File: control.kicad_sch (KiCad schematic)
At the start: 16 parts, among them J1 Wurth_THR_Terminal_M4, J2 Wurth_THR_Terminal_M4, J3 Wurth_THR_Terminal_M4, J5 Conn_02x20_Odd_Even, J6 TE_Faston_20-16AWG_Straight_T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, J7 TE_Faston_20-16AWG_Straight_T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, U1 TPS7B8733, U2 MAX33071

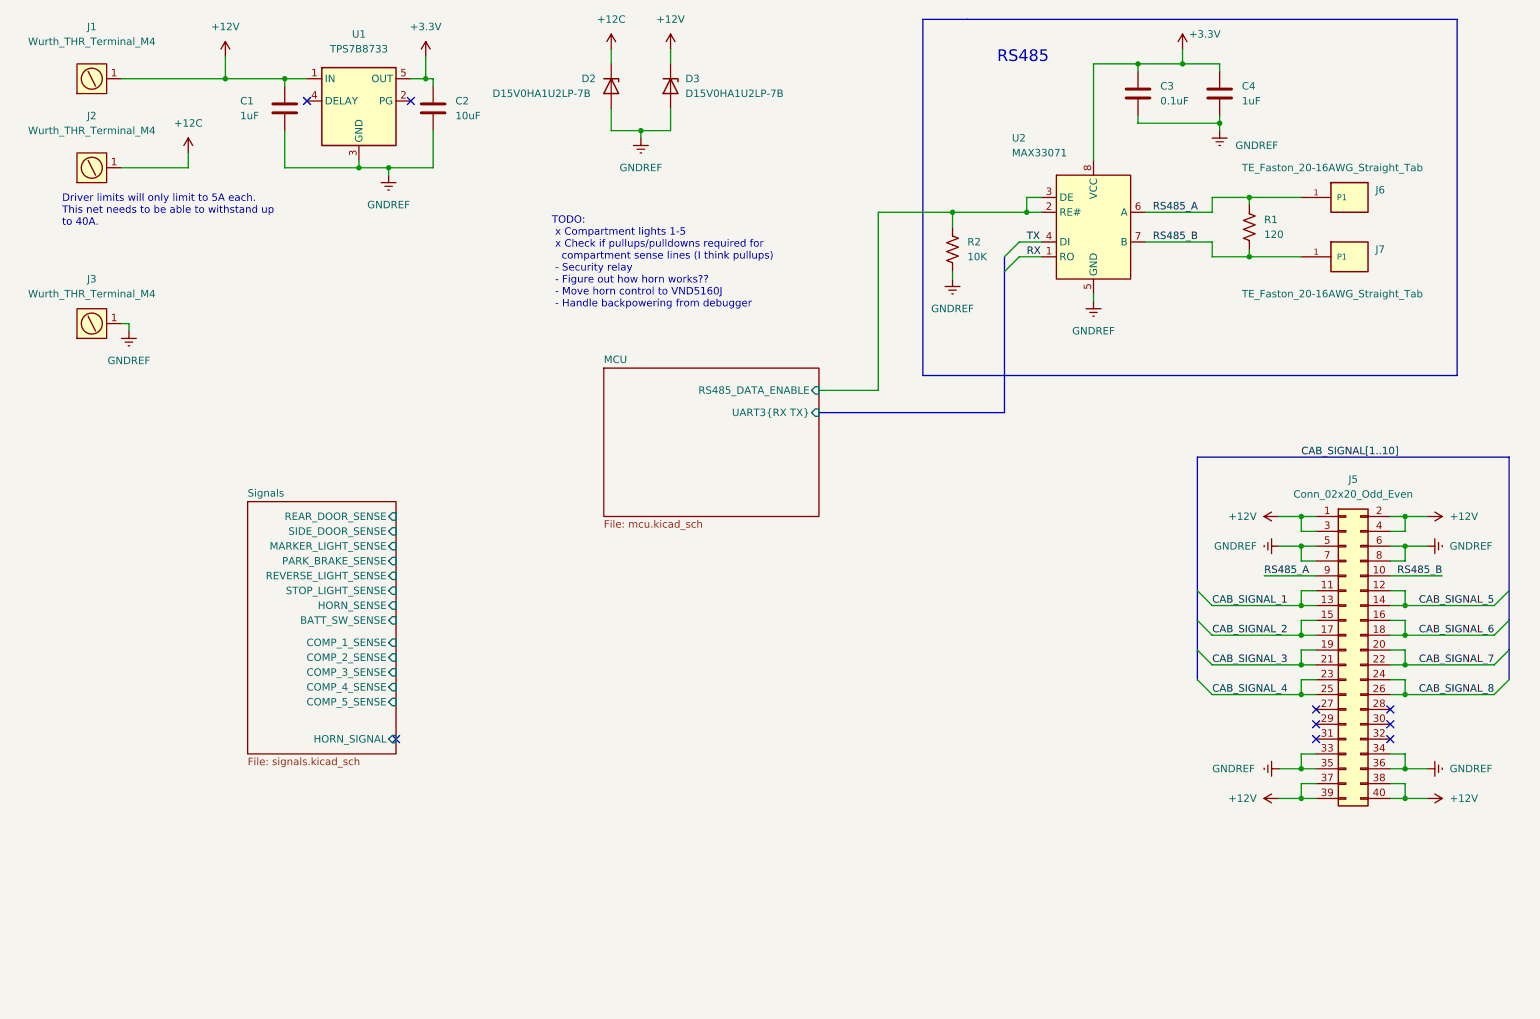
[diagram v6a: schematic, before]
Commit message: add cab signals and connect inputs
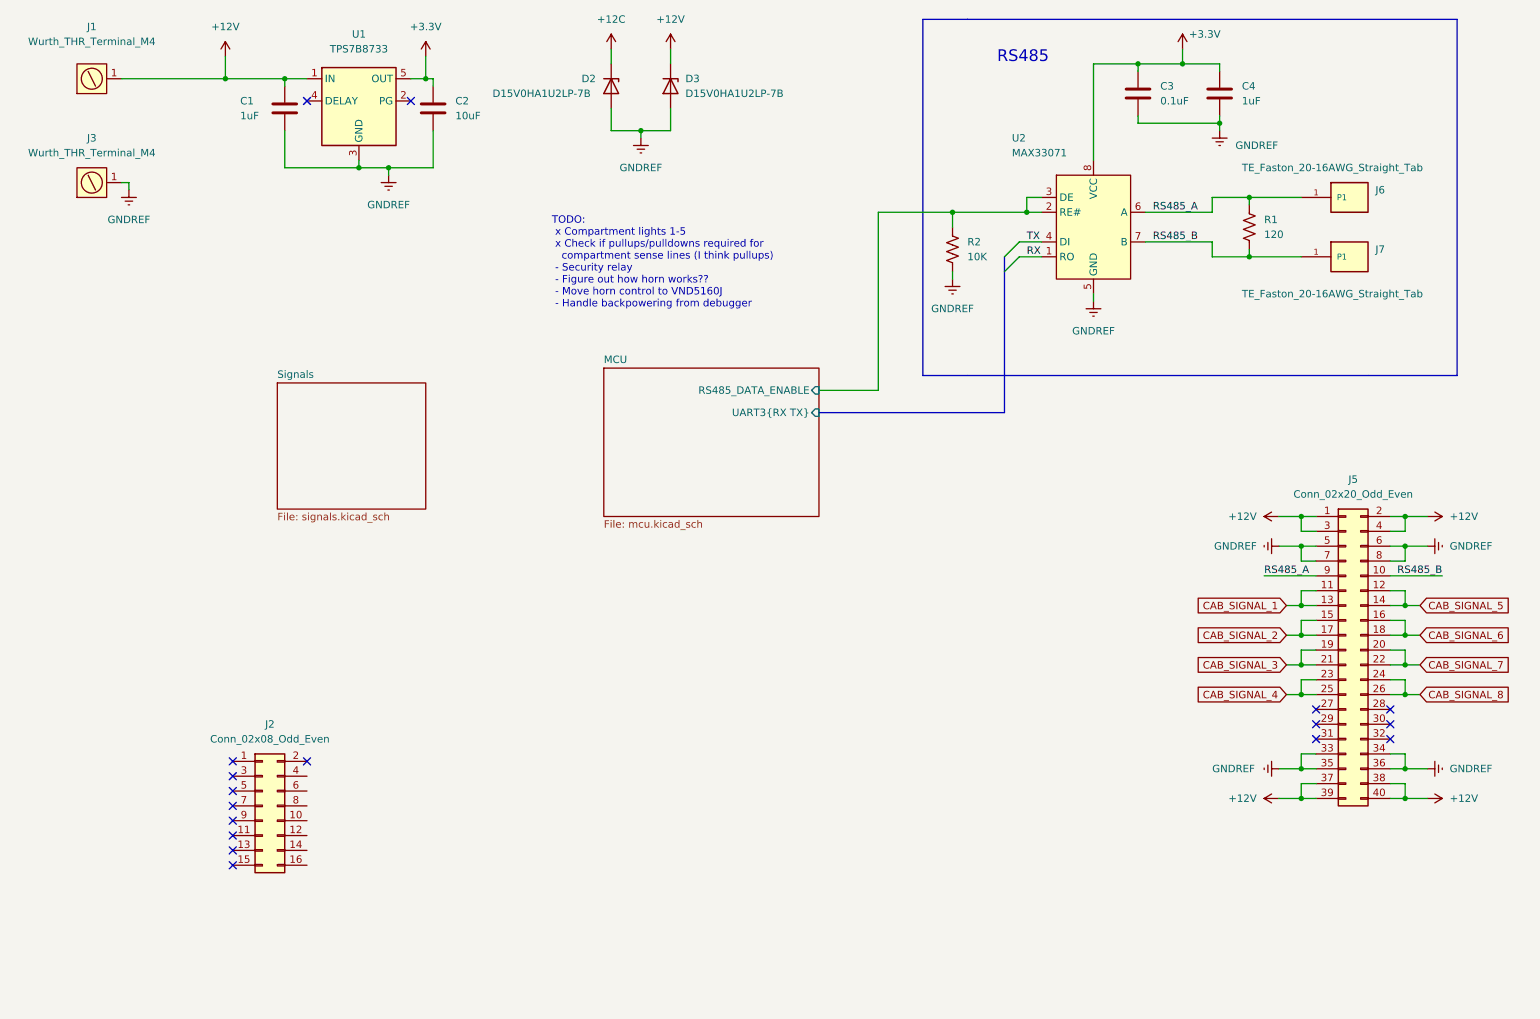
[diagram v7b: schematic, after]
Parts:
- removed J2: Wurth_THR_Terminal_M4, Toadly:Wurth_THR_Terminal_M4, symbol Toadly:Wurth_THR_Terminal_M4
- added J2: Conn_02x08_Odd_Even, Connector_PinHeader_2.54mm:PinHeader_2x08_P2.54mm_Vertical, symbol Connector_Generic:Conn_02x08_Odd_Even
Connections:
- no-connect marks 9 -> 17
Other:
- sheet Signals ports: added none; removed BATT_SW_SENSE, COMP_1_SENSE, COMP_2_SENSE, COMP_3_SENSE, COMP_4_SENSE, COMP_5_SENSE, HORN_SENSE, HORN_SIGNAL, MARKER_LIGHT_SENSE, PARK_BRAKE_SENSE, REAR_DOOR_SENSE, REVERSE_LIGHT_SENSE, SIDE_DOOR_SENSE, STOP_LIGHT_SENSE
- note removed: "Driver limits will only limit to 5A each. This net needs to be able to withstand up to 40A."
- moved on the sheet: J3

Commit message: connect signals to connectors, start layout
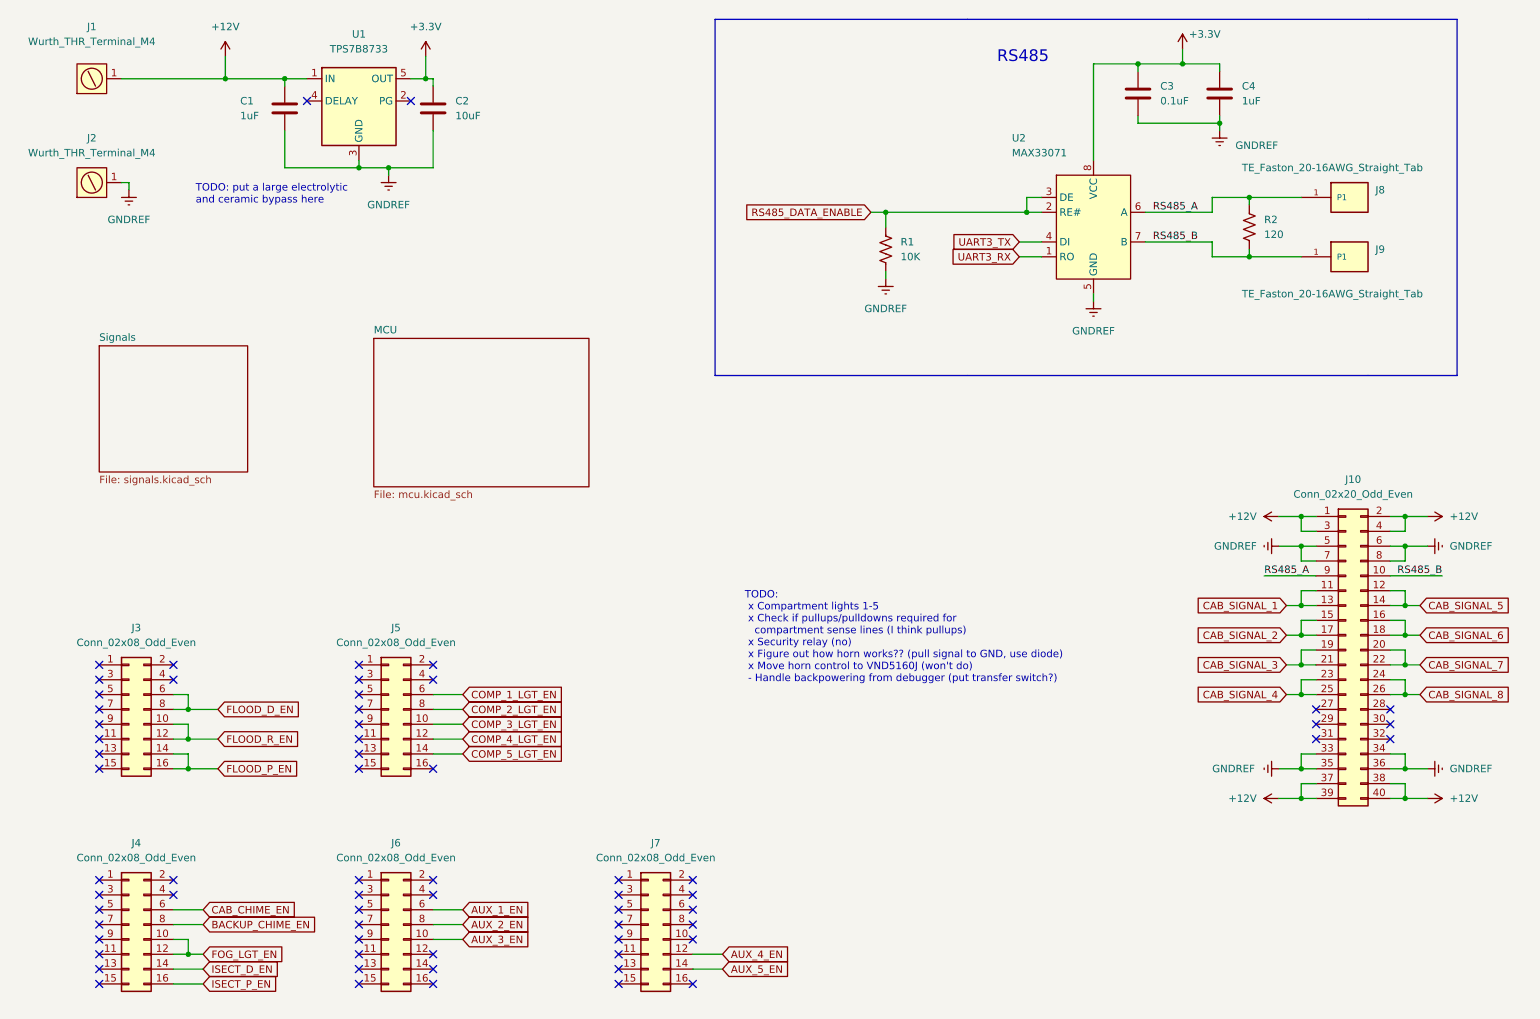
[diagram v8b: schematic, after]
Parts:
- removed D2, D3: D15V0HA1U2LP-7B, Diode_SMD:D_0402_1005Metric_Pad0.77x0.64mm_HandSolder, symbol Device:D_Zener
- added J4, J5, J6, J7: Conn_02x08_Odd_Even, Connector_PinHeader_2.54mm:PinHeader_2x08_P2.54mm_Vertical, symbol Connector_Generic:Conn_02x08_Odd_Even
- renumbered J5 to J10, J3 to J2, J2 to J3, J6 to J8, J7 to J9, R2 to R1, R1 to R2
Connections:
- net FLOOD_R_EN: now reaches J3.10 (Pin_10)
- net FLOOD_R_EN: now also J3.12 (Pin_12)
- net FLOOD_P_EN: now reaches J3.14 (Pin_14)
- net FLOOD_P_EN: now also J3.16 (Pin_16)
- net FLOOD_D_EN: now reaches J3.6 (Pin_6)
- net FLOOD_D_EN: now also J3.8 (Pin_8)
- net MCU/RS485_DATA_ENABLE renamed RS485_DATA_ENABLE
- net RX renamed UART3_RX
- net TX renamed UART3_TX
- new net AUX_1_EN: J6.6 (Pin_6)
- new net AUX_2_EN: J6.8 (Pin_8)
- new net AUX_3_EN: J6.10 (Pin_10)
- new net AUX_4_EN: J7.12 (Pin_12)
- new net AUX_5_EN: J7.14 (Pin_14)
- new net BACKUP_CHIME_EN: J4.8 (Pin_8)
- new net CAB_CHIME_EN: J4.6 (Pin_6)
- new net COMP_1_LGT_EN: J5.6 (Pin_6)
- new net COMP_2_LGT_EN: J5.8 (Pin_8)
- new net COMP_3_LGT_EN: J5.10 (Pin_10)
- new net COMP_4_LGT_EN: J5.12 (Pin_12)
- new net COMP_5_LGT_EN: J5.14 (Pin_14)
- new net FOG_LGT_EN: J4.10 (Pin_10), J4.12 (Pin_12)
- new net ISECT_D_EN: J4.14 (Pin_14)
- new net ISECT_P_EN: J4.16 (Pin_16)
- no-connect marks 17 -> 66
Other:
- sheet MCU ports: added none; removed RS485_DATA_ENABLE, UART3{RX TX}
- note added: "TODO: put a large electrolytic and ceramic bypass here"
- note added: "TODO: x Compartment lights 1-5 x Check if pullups/pulldowns required for compartment sense lines (I think pullups) x Security relay (no) x Figure out how horn works?? (pull signal to GND, use diode) x Move horn control to VND5160J (won't do) - Handle backpowering from debugger (put transfer switch?)"
- note removed: "TODO: x Compartment lights 1-5 x Check if pullups/pulldowns required for compartment sense lines (I think pullups) - Security relay - Figure out how horn works?? - Move horn control to VND5160J - Handle backpowering from debugger"
- moved on the sheet: J3, R1
